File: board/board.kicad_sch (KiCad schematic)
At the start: 34 parts, among them J1 ANT, J2 DEBUG, P1 USB_C_Plug_USB2.0, SW1 BOOTSEL, SW2 RUN, U1 RP2040, U2 W25Q128JVS, U3 NCP1117-3.3_SOT223, U4 RFM95W-915S2, Y1 ABM8G-12.000MHZ-18-D2Y-T

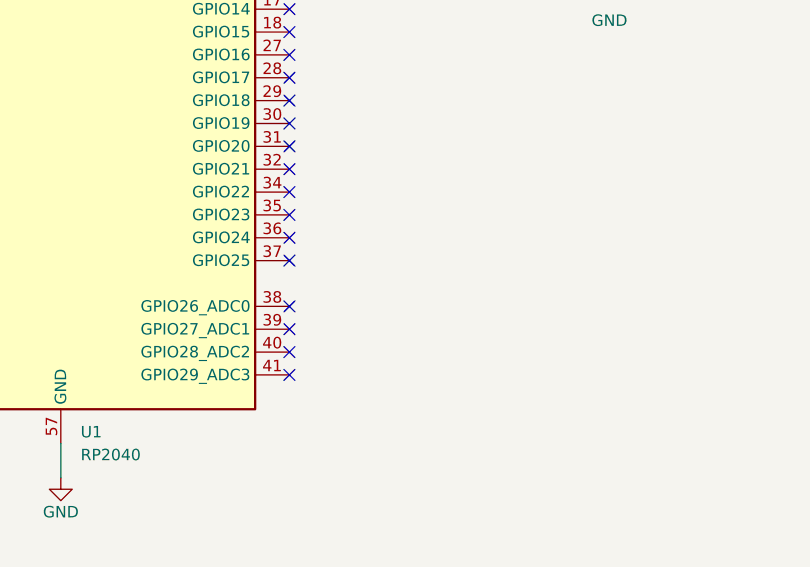
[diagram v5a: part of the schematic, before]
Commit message: add GPIO
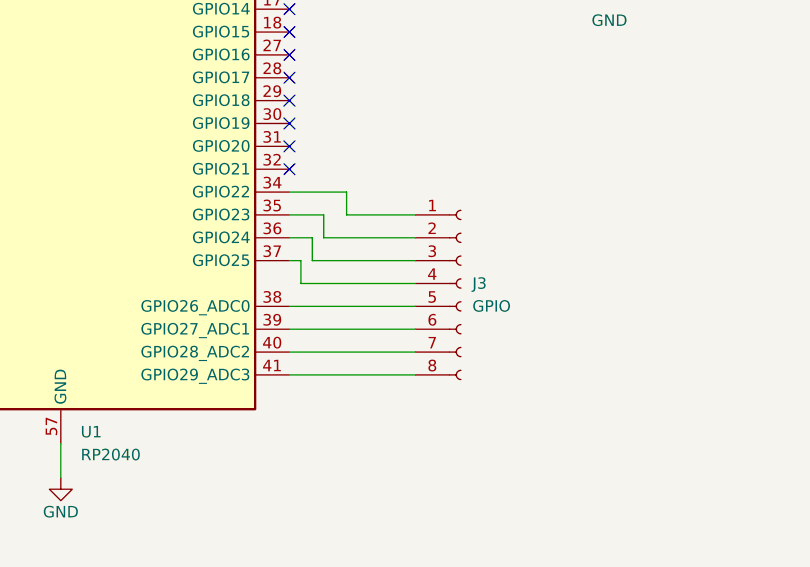
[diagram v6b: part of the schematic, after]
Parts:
- added J3: GPIO, Connector_PinSocket_2.54mm:PinSocket_1x08_P2.54mm_Vertical, symbol Connector:Conn_01x08_Socket
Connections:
- net at U1.34 (GPIO22): now also J3.1 (Pin_1)
- net at U1.35 (GPIO23): now also J3.2 (Pin_2)
- net at U1.36 (GPIO24): now also J3.3 (Pin_3)
- net at U1.37 (GPIO25): now also J3.4 (Pin_4)
- net at U1.38 (GPIO26_ADC0): now also J3.5 (Pin_5)
- net at U1.39 (GPIO27_ADC1): now also J3.6 (Pin_6)
- net at U1.40 (GPIO28_ADC2): now also J3.7 (Pin_7)
- net at U1.41 (GPIO29_ADC3): now also J3.8 (Pin_8)
- no-connect marks 19 -> 11
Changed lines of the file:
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@@
 	)
 	(no_connect
-		(at 115.57 125.73)
-	)
-	(no_connect
-		(at 115.57 128.27)
-	)
-	(no_connect
-		(at 115.57 113.03)
-	)
-	(no_connect
-		(at 115.57 120.65)
-	)
-	(no_connect
 		(at 115.57 87.63)
 	)
@@
 	)
 	(no_connect
-		(at 115.57 115.57)
-	)
-	(no_connect
-		(at 115.57 107.95)
-	)
-	(no_connect
 		(at 115.57 85.09)
 	)
 	(no_connect
-		(at 115.57 123.19)
-	)
-	(no_connect
 		(at 115.57 105.41)
 	)
@@
 		(at 115.57 95.25)
 	)
-	(no_connect
-		(at 115.57 110.49)
-	)
 	(wire
 		(pts
@@
 	(wire
 		(pts
+			(xy 118.11 113.03) (xy 118.11 115.57)
+		)
+		(stroke
+			(width 0)
+			(type default)
+		)
+	)
+	(wire
+		(pts
 			(xy 62.23 82.55) (xy 64.77 82.55)
 		)
@@
 	(wire
 		(pts
+			(xy 121.92 107.95) (xy 121.92 110.49)
+		)
+		(stroke
+			(width 0)
+			(type default)
+		)
+	)
+	(wire
+		(pts
 			(xy 163.83 57.15) (xy 180.34 57.15)
 		)
@@
 	(wire
 		(pts
+			(xy 115.57 110.49) (xy 119.38 110.49)
+		)
+		(stroke
+			(width 0)
+			(type default)
+		)
+	)
+	(wire
+		(pts
 			(xy 115.57 64.77) (xy 118.11 64.77)
 		)
@@
 	(wire
 		(pts
+			(xy 115.57 128.27) (xy 129.54 128.27)
+		)
+		(stroke
+			(width 0)
+			(type default)
+		)
+	)
+	(wire
+		(pts
 			(xy 85.09 41.91) (xy 73.66 41.91)
 		)
@@
 	(wire
 		(pts
+			(xy 118.11 115.57) (xy 129.54 115.57)
+		)
+		(stroke
+			(width 0)
+			(type default)
+		)
+	)
+	(wire
+		(pts
 			(xy 31.75 64.77) (xy 34.29 64.77)
 		)
@@
 	(wire
 		(pts
+			(xy 115.57 107.95) (xy 121.92 107.95)
+		)
+		(stroke
+			(width 0)
+			(type default)
+		)
+	)
+	(wire
+		(pts
 			(xy 31.75 64.77) (xy 31.75 78.74)
 		)
@@
 	(wire
 		(pts
+			(xy 116.84 115.57) (xy 116.84 118.11)
+		)
+		(stroke
+			(width 0)
+			(type default)
+		)
+	)
+	(wire
+		(pts
 			(xy 185.42 62.23) (xy 185.42 64.77)
 		)
@@
 	(wire
 		(pts
+			(xy 119.38 110.49) (xy 119.38 113.03)
+		)
+		(stroke
+			(width 0)
+			(type default)
+		)
+	)
+	(wire
+		(pts
 			(xy 64.77 27.94) (xy 54.61 27.94)
 		)
@@
 	(wire
 		(pts
+			(xy 115.57 115.57) (xy 116.84 115.57)
+		)
+		(stroke
+			(width 0)
+			(type default)
+		)
+	)
+	(wire
+		(pts
 			(xy 45.72 20.32) (xy 45.72 19.05)
 		)
@@
 	(wire
 		(pts
+			(xy 115.57 125.73) (xy 129.54 125.73)
+		)
+		(stroke
+			(width 0)
+			(type default)
+		)
+	)
+	(wire
+		(pts
+			(xy 116.84 118.11) (xy 129.54 118.11)
+		)
+		(stroke
+			(width 0)
+			(type default)
+		)
+	)
+	(wire
+		(pts
 			(xy 163.83 69.85) (xy 175.26 69.85)
 		)
@@
 	(wire
 		(pts
+			(xy 121.92 110.49) (xy 129.54 110.49)
+		)
+		(stroke
+			(width 0)
+			(type default)
+		)
+	)
+	(wire
+		(pts
 			(xy 43.18 21.59) (xy 46.99 21.59)
 		)
@@
 	(wire
 		(pts
+			(xy 119.38 113.03) (xy 129.54 113.03)
+		)
+		(stroke
+			(width 0)
+			(type default)
+		)
+	)
+	(wire
+		(pts
 			(xy 41.91 33.02) (xy 45.72 33.02)
 		)
@@
 	(wire
 		(pts
+			(xy 115.57 123.19) (xy 129.54 123.19)
+		)
+		(stroke
+			(width 0)
+			(type default)
+		)
+	)
+	(wire
+		(pts
 			(xy 101.6 20.32) (xy 104.14 20.32)
 		)
@@
 	(wire
 		(pts
+			(xy 115.57 113.03) (xy 118.11 113.03)
+		)
+		(stroke
+			(width 0)
+			(type default)
+		)
+	)
+	(wire
+		(pts
 			(xy 45.72 62.23) (xy 55.88 62.23)
 		)
@@
 	(wire
 		(pts
+			(xy 115.57 120.65) (xy 129.54 120.65)
+		)
+		(stroke
+			(width 0)
+			(type default)
+		)
+	)
+	(wire
+		(pts
 			(xy 54.61 35.56) (xy 54.61 34.29)
 		)
@@
 					(unit 1)
 				)
+			)
+		)
+	)
+	(symbol
+		(lib_id "Connector:Conn_01x08_Socket")
+		(at 134.62 118.11 0)
+		(unit 1)
+		(exclude_from_sim no)
+		(in_bom yes)
+		(on_board yes)
+		(dnp no)
+		(fields_autoplaced yes)
+		(property "Reference" "J3"
+			(at 135.89 118.1099 0)
+			(effects
+				(font
+					(size 1.27 1.27)
+				)
+				(justify left)
+			)
+		)
+		(property "Value" "GPIO"
+			(at 135.89 120.6499 0)
+			(effects
+				(font
+					(size 1.27 1.27)
+				)
+				(justify left)
+			)
+		)
+		(property "Footprint" "Connector_PinSocket_2.54mm:PinSocket_1x08_P2.54mm_Vertical"
+			(at 134.62 118.11 0)
+			(effects
+				(font
+					(size 1.27 1.27)
+				)
+				(hide yes)
+			)
+		)
+		(property "Datasheet" "~"
+			(at 134.62 118.11 0)
+			(effects
+				(font
+					(size 1.27 1.27)
+				)
+				(hide yes)
+			)
+		)
+		(property "Description" "Generic connector, single row, 01x08, script generated"
+			(at 134.62 118.11 0)
+			(effects
+				(font
+					(size 1.27 1.27)
+				)
+				(hide yes)
+			)
+		)
+		(pin "4"
+		)
+		(pin "6"
+		)
+		(pin "1"
+		)
+		(pin "3"
+		)
+		(pin "2"
+		)
+		(pin "5"
+		)
+		(pin "7"
+		)
+		(pin "8"
+		)
+		(instances
+			(project ""
+				(path "/6eb10beb-f31c-4c13-8f79-f4b6753787bf"
+					(reference "J3")
+					(unit 1)
+				)

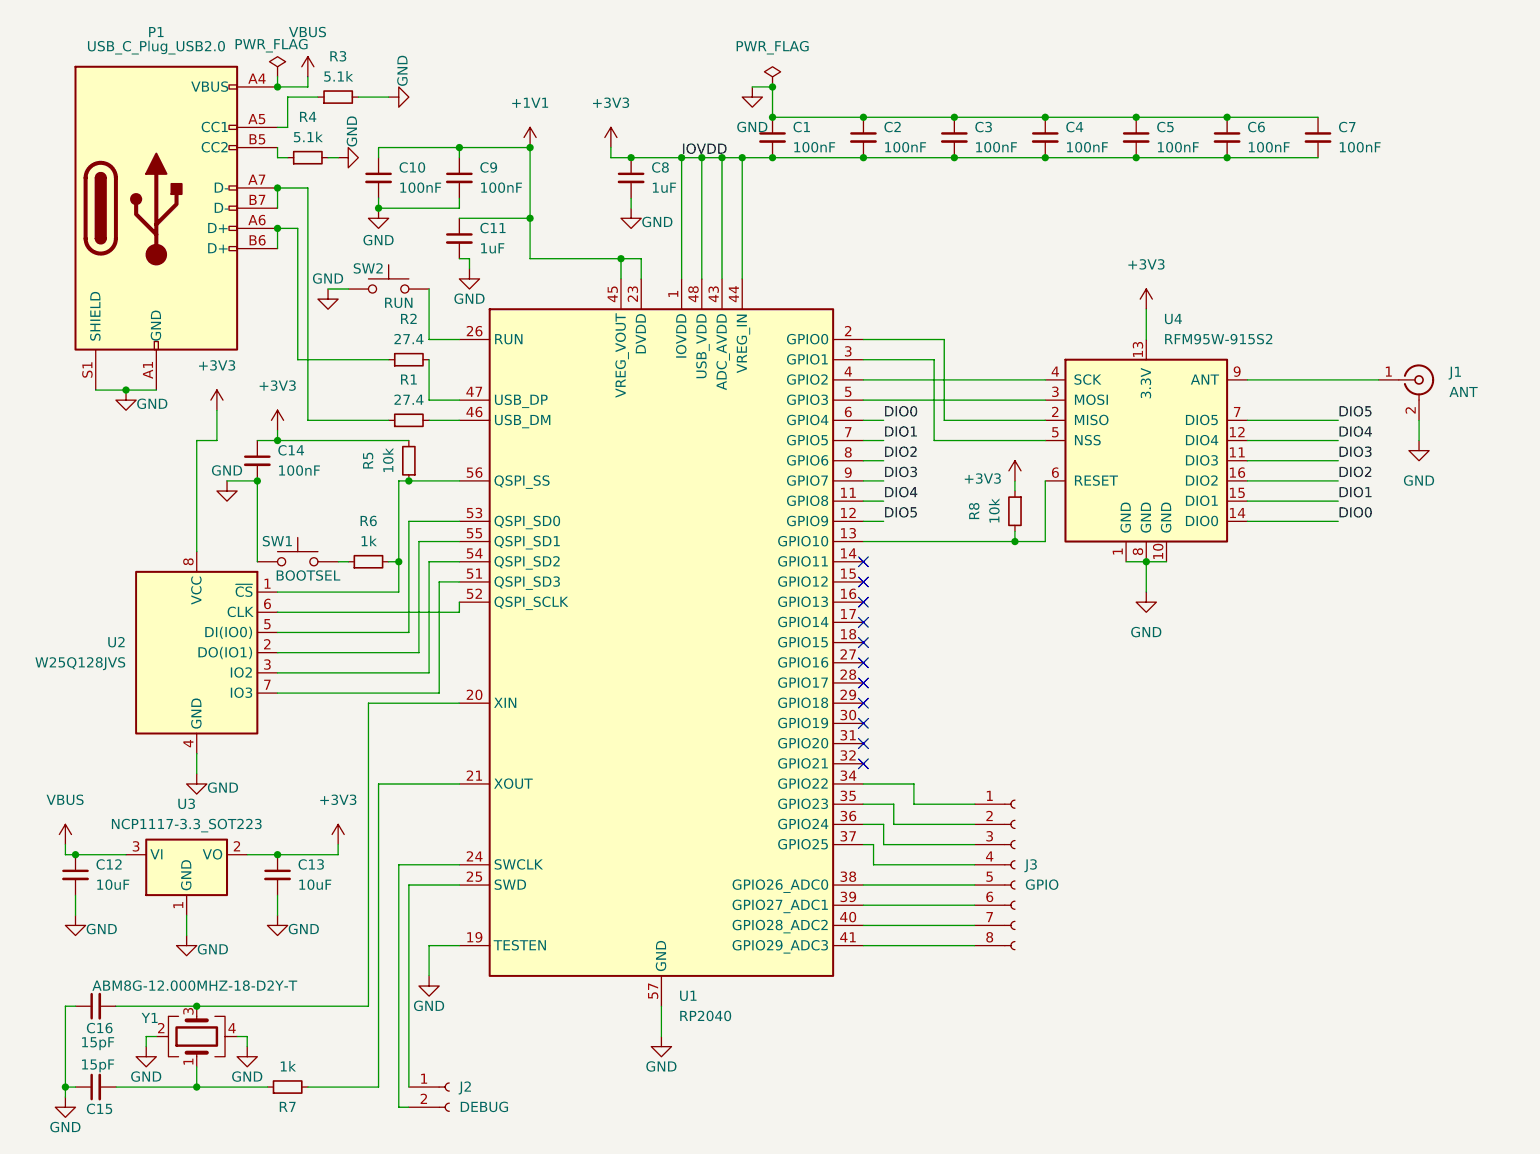
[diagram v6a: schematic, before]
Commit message: schematic v2 ft. ble, license under CC-BY-NC 4.0
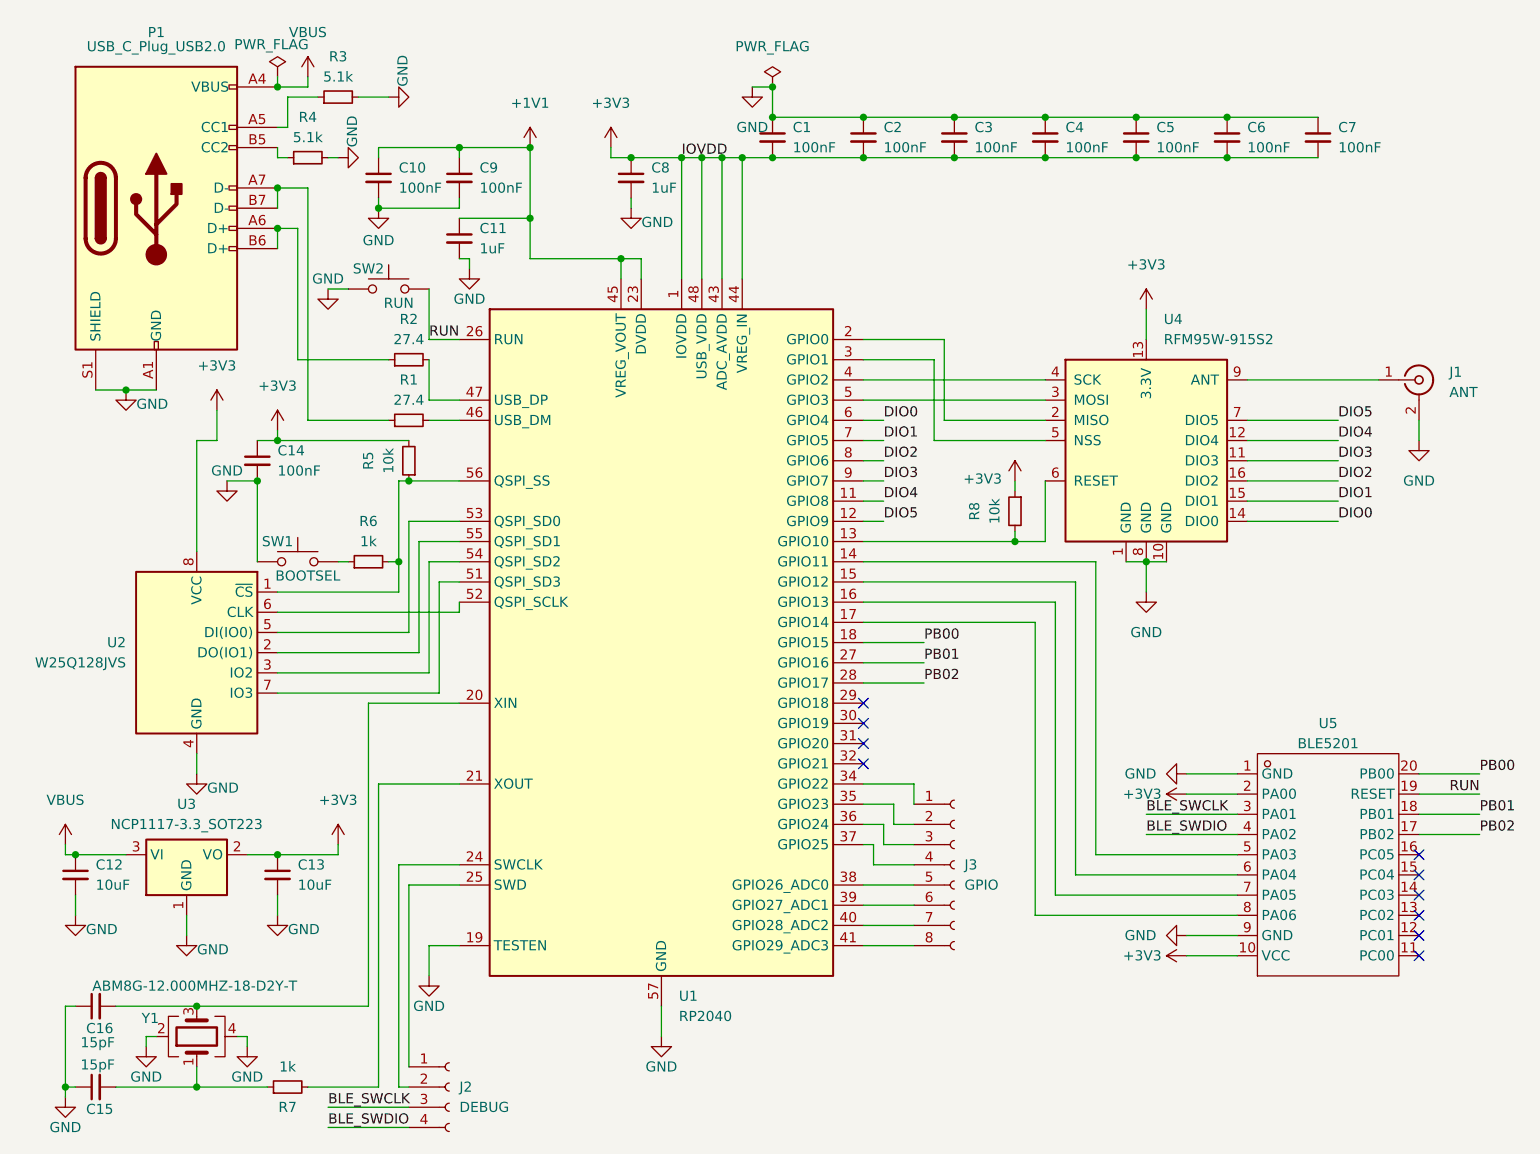
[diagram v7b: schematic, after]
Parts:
- added U5: BLE5201, BLE5201:BLE5201, symbol BLE5201:BLE5201
- J2: footprint Connector_PinSocket_2.54mm:PinSocket_1x02_P2.54mm_Vertical -> Connector_PinSocket_2.54mm:PinSocket_1x04_P2.54mm_Vertical; symbol Connector:Conn_01x02_Socket -> Connector:Conn_01x04_Socket
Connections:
- net +3V3: now also U5.10 (VCC), U5.2 (PA00)
- net GND: now also U5.1 (GND), U5.9 (GND)
- net RUN: now reaches SW2.2, U1.26 (RUN)
- net RUN: now also U5.19 (RESET)
- net at U1.14 (GPIO11): now also U5.5 (PA03)
- net at U1.15 (GPIO12): now also U5.6 (PA04)
- net at U1.16 (GPIO13): now also U5.7 (PA05)
- net at U1.17 (GPIO14): now also U5.8 (PA06)
- net PB00: now reaches U1.18 (GPIO15)
- net PB00: now also U5.20 (PB00)
- net PB01: now reaches U1.27 (GPIO16)
- net PB01: now also U5.18 (PB01)
- net PB02: now reaches U1.28 (GPIO17)
- net PB02: now also U5.17 (PB02)
- new net BLE_SWCLK: J2.3 (Pin_3), U5.3 (PA01)
- new net BLE_SWDIO: J2.4 (Pin_4), U5.4 (PA02)
- no-connect marks 11 -> 10
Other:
- title: (none) -> YARLoRa
- moved on the sheet: J3

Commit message: board v2 hour 1
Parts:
- J3: footprint Connector_PinSocket_2.54mm:PinSocket_1x08_P2.54mm_Vertical -> Connector_PinSocket_2.54mm:PinSocket_1x12_P2.54mm_Vertical; symbol Connector:Conn_01x08_Socket -> Connector:Conn_01x12_Socket
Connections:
- net PC00: now reaches U5.11 (PC00)
- net PC00: now also J3.9 (Pin_9)
- net PC01: now reaches U5.12 (PC01)
- net PC01: now also J3.10 (Pin_10)
- net PC02: now reaches U5.13 (PC02)
- net PC02: now also J3.11 (Pin_11)
- net PC03: now reaches U5.14 (PC03)
- net PC03: now also J3.12 (Pin_12)
- no-connect marks 10 -> 6
